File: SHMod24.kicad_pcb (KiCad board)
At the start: 2 copper layers, 49.5 x 49.5 mm, 34 parts, among them IC1 ArduinoProMini, J1 Conn_01x01, J2 Conn_01x01, J3 Conn_01x01, J4 Conn_01x01, Q1 FS8205A, U1 ESP-12, U2 NRF24L01, U3 AP2112K-3.3, U4 TP4056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

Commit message: NRF ESP Jumper
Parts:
- removed J2, J3, J4: Conn_01x01, Pin_Headers:Pin_Header_Straight_1x01_Pitch2.54mm
- added J5: 12V, Connectors_Terminal_Blocks:TerminalBlock_Pheonix_MKDS1.5-2pol, B.Cu at (55.5, 96.5)
- added JP3: Jumper_DeepSleep, LeoDJ-kicad:SOLDER-JUMPER_1-WAY, F.Cu at (95.8, 136.6)
- added JP4: ESP NRF, LeoDJ-kicad:SOLDER-JUMPER_2-WAY, F.Cu at (75.6, 80.8)
- added JP5: ESP NRF, LeoDJ-kicad:SOLDER-JUMPER_2-WAY, F.Cu at (75.6, 82.5)
- added JP6: ESP NRF, LeoDJ-kicad:SOLDER-JUMPER_2-WAY, F.Cu at (75.6, 79.0)
- added JP7: ESP NRF, LeoDJ-kicad:SOLDER-JUMPER_2-WAY, F.Cu at (75.6, 77.2)
- added JP8: ESP NRF, LeoDJ-kicad:SOLDER-JUMPER_2-WAY, F.Cu at (75.6, 75.4)
- added R11: 10k, Resistors_SMD:R_0805_HandSoldering, F.Cu at (107.7, 126.8)
- C1, C2, C3, C5, C6, C8, D1, JP1, L1, Q1, R10, R6, R7, R8, R9, U3, U4, U5, U6: moved to B.Cu
- J1: value Conn_01x01 -> Conn_02x06_Odd_Even; footprint Pin_Headers:Pin_Header_Straight_1x01_Pitch2.54mm -> Pin_Headers:Pin_Header_Straight_2x06_Pitch2.54mm_SMD
- moved J1 37.3 mm to (75.9, 105.7), turned to 90 degrees
- moved C7 34.3 mm to (59.2, 94.2), turned to 270 degrees
- moved C3 25.9 mm to (71.0, 106.8)
- moved C4 22.5 mm to (102.6, 126.8)
- moved R7 18.3 mm to (74.8, 109.9), turned to 180 degrees
- moved U5 18.3 mm to (74.8, 106.8), turned to 180 degrees
- moved C9 18.1 mm to (95.2, 129.6)
- moved Q1 17.8 mm to (75.1, 101.5), turned to 180 degrees
- moved R10 14.8 mm to (52.6, 106.5)
- moved R9 14.8 mm to (52.6, 103.3)
- moved C2 12.4 mm to (65.7, 97.5)
- moved C1 12.2 mm to (65.7, 91.2)
- moved R6 11.0 mm to (80.1, 96.4), turned to 270 degrees
- moved U4 10.7 mm to (75.1, 96.4), turned to 180 degrees
- moved JP1 10.5 mm to (69.3, 94.4), turned to 270 degrees
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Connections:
- net +VDC renamed P01
- net Net-(C6-Pad2) renamed /SW
- net Net-(R4-Pad2) renamed ADC
- U1 pad 10: Net-(U1-Pad10) -> GPIO15
- U1 pad 4: Net-(U1-Pad4) -> GPIO16
- U1 pad 5: Net-(U1-Pad5) -> GPIO14
- U1 pad 6: Net-(U1-Pad6) -> GPIO12
- U1 pad 7: Net-(U1-Pad7) -> GPIO13
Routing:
- net GPIO15: track 0.00 -> 32.4 mm, vias 0 -> 1
- net GPIO13: track 0.00 -> 12.2 mm, vias 0 -> 1
- net SCK: track 12.1 -> 23.0 mm
- net MISO: track 16.4 -> 27.0 mm, vias 0 -> 1
- net MOSI: track 20.4 -> 30.4 mm
- net GPIO14: track 0.00 -> 7.82 mm, vias 0 -> 1
- net GPIO16: track 0.00 -> 7.68 mm, vias 0 -> 1
- net GPIO12: track 0.00 -> 7.53 mm, vias 0 -> 1
- net Net-(Q1-Pad4): track 4.18 -> 9.99 mm
- net A0: track 20.6 -> 25.2 mm
- net /SW: track 13.6 -> 16.9 mm
- net SDA: track 39.4 -> 42.2 mm
- net +12V: track 13.4 -> 11.2 mm
- net SCL: track 36.3 -> 38.1 mm
- net TX: track 46.8 -> 47.8 mm
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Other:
- net class Power added: clearance 0.2, trace_width 0.4, via_dia 0.6, via_drill 0.4

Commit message: migrate to KiCad5 && further layouting
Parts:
- added ?: MountingHole_3.2mm_M3, Mounting_Holes:MountingHole_3.2mm_M3, F.Cu at (75.6, 65.4)
- added ?: MountingHole_3.2mm_M3, Mounting_Holes:MountingHole_3.2mm_M3, F.Cu at (54.0, 108.6)
- added ?: MountingHole_3.2mm_M3, Mounting_Holes:MountingHole_3.2mm_M3, F.Cu at (97.2, 108.6)
- added C10: 10µF, Capacitor_SMD:C_0805_2012Metric, F.Cu at (86.4, 84.1)
- added D2: LED, LED_SMD:LED_0805_2012Metric, B.Cu at (69.4, 101.6)
- added J2: Conn_01x01, Connector_Wire:SolderWirePad_1x01_Drill0.8mm, F.Cu at (52.8, 103.9)
- added J3: Conn_01x01, Connector_Wire:SolderWirePad_1x01_Drill0.8mm, F.Cu at (52.8, 100.8)
- added R12: 10k, Resistor_SMD:R_0805_2012Metric, F.Cu at (57.8, 117.8)
- added R13: 10k, Resistor_SMD:R_0805_2012Metric, F.Cu at (61.6, 117.8)
- added R14: 1k, Resistor_SMD:R_0805_2012Metric, B.Cu at (72.8, 101.6)
- added U7: NRF24L01, mysensors_radios:NRF24L01-SMD, F.Cu at (90.8, 63.9)
- C1, C2, C3: footprint Capacitors_SMD:C_0805_HandSoldering -> Capacitor_SMD:C_0805_2012Metric
- C4: footprint Capacitors_SMD:C_0805_HandSoldering -> Capacitor_SMD:C_0805_2012Metric; moved to B.Cu
- C5, C6: footprint Capacitors_SMD:C_0805 -> Capacitor_SMD:C_0805_2012Metric
- C7, C8: footprint Capacitors_SMD:C_1210 -> Capacitor_SMD:C_1210_3225Metric
- C9: footprint Capacitors_SMD:CP_Elec_6.3x5.8 -> Capacitor_SMD:CP_Elec_6.3x5.8
- D1: footprint Diodes_SMD:D_SMA -> Diode_SMD:D_SMA
- J1: footprint Pin_Headers:Pin_Header_Straight_2x06_Pitch2.54mm_SMD -> Connector_PinHeader_2.54mm:PinHeader_2x06_P2.54mm_Vertical_SMD
- J5: footprint Connectors_Terminal_Blocks:TerminalBlock_Pheonix_MKDS1.5-2pol -> TerminalBlock_Phoenix:TerminalBlock_Phoenix_MKDS-1,5-2_1x02_P5.00mm_Horizontal
- JP1: footprint jumper:SOLDER-JUMPER_2-WAY -> LeoDJ-kicad:SOLDER-JUMPER_2-WAY
- L1: footprint LeoDJ:L_0630 -> LeoDJ-kicad:L_0630
- Q1: footprint Housings_SSOP:TSSOP-8_4.4x3mm_Pitch0.65mm -> Package_SO:TSSOP-8_4.4x3mm_P0.65mm
- R1, R11, R2, R3, R4, R5, R6, R7, R8: footprint Resistors_SMD:R_0805_HandSoldering -> Resistor_SMD:R_0805_2012Metric
- R10, R9: footprint Resistors_SMD:R_0805 -> Resistor_SMD:R_0805_2012Metric
- U3: footprint TO_SOT_Packages_SMD:SOT-23-5 -> Package_TO_SOT_SMD:SOT-23-5
- U4: footprint Housings_SOIC:SOIC-8_3.9x4.9mm_Pitch1.27mm -> Package_SO:SOIC-8_3.9x4.9mm_P1.27mm
- U5, U6: footprint TO_SOT_Packages_SMD:SOT-23-6_Handsoldering -> Package_TO_SOT_SMD:SOT-23-6_Handsoldering
- moved JP3 66.3 mm to (72.1, 74.7), turned to 270 degrees
- moved R11 61.5 mm to (61.3, 86.4), turned to 180 degrees
- moved C9 46.4 mm to (65.8, 93.7), turned to 90 degrees
- moved C4 40.8 mm to (65.9, 109.1), turned to 270 degrees
- moved R10 27.0 mm to (76.1, 93.2), turned to 90 degrees
- moved C6 24.8 mm to (72.7, 90.5), turned to 180 degrees
- moved R9 24.5 mm to (76.1, 96.5), turned to 90 degrees
- moved U6 21.0 mm to (72.7, 93.3), turned to 180 degrees
- moved D1 19.3 mm to (67.2, 90.5), turned to 180 degrees
- moved C8 17.7 mm to (72.7, 96.7), turned to 0 degrees
- moved C2 16.3 mm to (81.0, 102.9), turned to 270 degrees
- moved C1 15.4 mm to (75.7, 102.9), turned to 270 degrees
- moved U3 15.3 mm to (78.4, 102.9), turned to 90 degrees
- moved R8 13.0 mm to (65.9, 105.5)
- moved Q1 13.0 mm to (62.1, 102.0)
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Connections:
- net +12V renamed VCC
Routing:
- net +BATT: track 0.00 -> 47.8 mm
- net N24_CS: track 13.8 -> 38.8 mm, vias 2 -> 3
- net N24_CE: track 14.4 -> 37.9 mm, vias 1 -> 2
- net VCC: track 11.2 -> 31.1 mm
- net MOSI: track 30.4 -> 39.4 mm
- net SCK: track 23.0 -> 31.5 mm
- net MISO: track 27.0 -> 35.5 mm
- net +5V: track 32.9 -> 39.8 mm, vias 0 -> 1
- net Net-(D2-Pad1): track 0.00 -> 5.94 mm
- net GPIO16: track 7.68 -> 12.9 mm, vias 1 -> 2
- net Net-(JP3-Pad1): track 0.00 -> 4.19 mm, vias 0 -> 1
- net -BATT: track 16.6 -> 19.8 mm
- net GPIO15: track 32.4 -> 35.6 mm
- net A0: track 25.2 -> 28.1 mm
- net GND: track 64.4 -> 62.1 mm, vias 1 -> 5
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- added copper zone on F.Cu, net GND

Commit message: more layouting
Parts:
- removed ? (x3): MountingHole_3.2mm_M3, Mounting_Holes:MountingHole_3.2mm_M3
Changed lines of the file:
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@@
     (tracks 431)
     (zones 0)
-    (modules 50)
+    (modules 47)
     (nets 74)
   )
@@
     )
   )
-  (module Mounting_Holes:MountingHole_3.2mm_M3 (layer F.Cu)
-    (at 75.565 65.405)
-    (descr "Mounting Hole 3.2mm, no annular, M3")
-    (tags "mounting hole 3.2mm no annular m3")
-    (attr virtual)
-    (fp_text reference "" (at 0 -4.2) (layer F.SilkS)
-      (effects (font (size 1 1) (thickness 0.15)))
-    )
-    (fp_text value MountingHole_3.2mm_M3 (at 0 4.2) (layer F.Fab)
-      (effects (font (size 1 1) (thickness 0.15)))
-    )
-    (fp_text user %R (at 0.3 0) (layer F.Fab)
-      (effects (font (size 1 1) (thickness 0.15)))
-    )
-    (fp_circle (center 0 0) (end 3.2 0) (layer Cmts.User) (width 0.15))
-    (fp_circle (center 0 0) (end 3.45 0) (layer F.CrtYd) (width 0.05))
-    (pad 1 np_thru_hole circle (at 0 0) (size 3.2 3.2) (drill 3.2) (layers *.Cu *.Mask))
-  )
-  (module Mounting_Holes:MountingHole_3.2mm_M3 (layer F.Cu)
-    (at 53.975 108.585)
-    (descr "Mounting Hole 3.2mm, no annular, M3")
-    (tags "mounting hole 3.2mm no annular m3")
-    (attr virtual)
-    (fp_text reference "" (at 0 -4.2) (layer F.SilkS)
-      (effects (font (size 1 1) (thickness 0.15)))
-    )
-    (fp_text value MountingHole_3.2mm_M3 (at 0 4.2) (layer F.Fab)
-      (effects (font (size 1 1) (thickness 0.15)))
-    )
-    (fp_text user %R (at 0.3 0) (layer F.Fab)
-      (effects (font (size 1 1) (thickness 0.15)))
-    )
-    (fp_circle (center 0 0) (end 3.2 0) (layer Cmts.User) (width 0.15))
-    (fp_circle (center 0 0) (end 3.45 0) (layer F.CrtYd) (width 0.05))
-    (pad 1 np_thru_hole circle (at 0 0) (size 3.2 3.2) (drill 3.2) (layers *.Cu *.Mask))
-  )
   (module mysensors_arduino:pro_mini (layer B.Cu)
     (at 90.805 80.01 270)
@@
     (pad 2 smd rect (at 0 0) (size 1 1) (layers F.Cu F.Paste F.Mask)
       (net 51 GPIO15))
-  )
-  (module Mounting_Holes:MountingHole_3.2mm_M3 (layer F.Cu)
-    (at 97.155 108.585)
-    (descr "Mounting Hole 3.2mm, no annular, M3")
-    (tags "mounting hole 3.2mm no annular m3")
-    (attr virtual)
-    (fp_text reference "" (at 0 -4.2) (layer F.SilkS)
-      (effects (font (size 1 1) (thickness 0.15)))
-    )
-    (fp_text value MountingHole_3.2mm_M3 (at 0 4.2) (layer F.Fab)
-      (effects (font (size 1 1) (thickness 0.15)))
-    )
-    (fp_text user %R (at 0.3 0) (layer F.Fab)
-      (effects (font (size 1 1) (thickness 0.15)))
-    )
-    (fp_circle (center 0 0) (end 3.2 0) (layer Cmts.User) (width 0.15))
-    (fp_circle (center 0 0) (end 3.45 0) (layer F.CrtYd) (width 0.05))
-    (pad 1 np_thru_hole circle (at 0 0) (size 3.2 3.2) (drill 3.2) (layers *.Cu *.Mask))
   )
   (module Capacitor_SMD:C_0805_2012Metric (layer B.Cu)
@@
   (segment (start 74.0575 91.7105) (end 74.0575 92.3315) (width 0.25) (layer B.Cu) (net 48))
   (segment (start 73.7075 91.3605) (end 74.0575 91.7105) (width 0.25) (layer B.Cu) (net 48))
-  (segment (start 71.3575 93.2815) (end 71.3575 94.2315) (width 0.4) (layer B.Cu) (net 71))
-  (segment (start 59.262 91.52) (end 55.499 91.52) (width 0.4) (layer B.Cu) (net 71))
-  (segment (start 60.706 92.964) (end 59.262 91.52) (width 0.4) (layer B.Cu) (net 71))
-  (segment (start 71.3575 93.2815) (end 66.6115 93.2815) (width 0.4) (layer B.Cu) (net 71))
-  (segment (start 64.77 95.123) (end 64.77 97.79) (width 0.4) (layer B.Cu) (net 71))
-  (segment (start 66.6115 93.2815) (end 64.77 95.123) (width 0.4) (layer B.Cu) (net 71))
-  (segment (start 64.77 97.79) (end 64.008 98.552) (width 0.4) (layer B.Cu) (net 71))
-  (segment (start 64.008 98.552) (end 61.468 98.552) (width 0.4) (layer B.Cu) (net 71))
-  (segment (start 60.706 97.79) (end 60.706 92.964) (width 0.4) (layer B.Cu) (net 71))
-  (segment (start 61.468 98.552) (end 60.706 97.79) (width 0.4) (layer B.Cu) (net 71))
-  (segment (start 57.337477 91.52) (end 55.499 91.52) (width 0.4) (layer F.Cu) (net 71))
-  (segment (start 58.908 91.52) (end 57.337477 91.52) (width 0.4) (layer F.Cu) (net 71))
-  (segment (start 59.182 91.794) (end 58.908 91.52) (width 0.4) (layer F.Cu) (net 71))
-  (segment (start 59.182 92.804) (end 59.182 91.794) (width 0.4) (layer F.Cu) (net 71))
   (segment (start 76.1365 93.8505) (end 76.1365 95.1255) (width 0.25) (layer B.Cu) (net 49))
   (segment (start 74.191 94.098) (end 74.0575 94.2315) (width 0.25) (layer B.Cu) (net 49))
@@
   (segment (start 68.8975 74.6125) (end 68.8975 74.7075) (width 0.25) (layer B.Cu) (net 69) (status 30))
   (segment (start 60.0875 74.6125) (end 63.7375 74.6125) (width 0.25) (layer F.Cu) (net 69))
+  (segment (start 71.3575 93.2815) (end 71.3575 94.2315) (width 0.4) (layer B.Cu) (net 71))
+  (segment (start 59.262 91.52) (end 55.499 91.52) (width 0.4) (layer B.Cu) (net 71))
+  (segment (start 60.706 92.964) (end 59.262 91.52) (width 0.4) (layer B.Cu) (net 71))
+  (segment (start 71.3575 93.2815) (end 66.6115 93.2815) (width 0.4) (layer B.Cu) (net 71))
+  (segment (start 64.77 95.123) (end 64.77 97.79) (width 0.4) (layer B.Cu) (net 71))
+  (segment (start 66.6115 93.2815) (end 64.77 95.123) (width 0.4) (layer B.Cu) (net 71))
+  (segment (start 64.77 97.79) (end 64.008 98.552) (width 0.4) (layer B.Cu) (net 71))
+  (segment (start 64.008 98.552) (end 61.468 98.552) (width 0.4) (layer B.Cu) (net 71))
+  (segment (start 60.706 97.79) (end 60.706 92.964) (width 0.4) (layer B.Cu) (net 71))
+  (segment (start 61.468 98.552) (end 60.706 97.79) (width 0.4) (layer B.Cu) (net 71))
+  (segment (start 57.337477 91.52) (end 55.499 91.52) (width 0.4) (layer F.Cu) (net 71))
+  (segment (start 58.908 91.52) (end 57.337477 91.52) (width 0.4) (layer F.Cu) (net 71))
+  (segment (start 59.182 91.794) (end 58.908 91.52) (width 0.4) (layer F.Cu) (net 71))
+  (segment (start 59.182 92.804) (end 59.182 91.794) (width 0.4) (layer F.Cu) (net 71))
   (segment (start 68.5165 106.807) (end 67.7545 106.045) (width 0.25) (layer B.Cu) (net 72))
   (segment (start 68.9915 106.807) (end 68.5165 106.807) (width 0.25) (layer B.Cu) (net 72))

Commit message: even more layouting
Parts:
- J1: value Conn_02x06_Odd_Even -> Conn_02x14_Odd_Even; footprint Connector_PinHeader_2.54mm:PinHeader_2x06_P2.54mm_Vertical_SMD -> Connector_PinHeader_2.54mm:PinHeader_2x14_P2.54mm_Vertical_SMD
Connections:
- IC1 pad 12: Net-(IC1-Pad12) -> P09
- IC1 pad 13: Net-(IC1-Pad13) -> P10
- IC1 pad 18: Net-(IC1-Pad18) -> A1
- IC1 pad 19: Net-(IC1-Pad19) -> A2
- IC1 pad 20: Net-(IC1-Pad20) -> A3
- IC1 pad 5: Net-(IC1-Pad5) -> P02
- IC1 pad 6: Net-(IC1-Pad6) -> P03
- IC1 pad 7: Net-(IC1-Pad7) -> P04
- IC1 pad 8: Net-(IC1-Pad8) -> P05
- IC1 pad 9: Net-(IC1-Pad9) -> P06
- J1 pad 1: P01 -> GND
- J1 pad 10: P08 -> SCL
- J1 pad 11: P06 -> MISO
- J1 pad 12: P07 -> MOSI
- J1 pad 2: Net-(J1-Pad2) -> GND
- J1 pad 3: P02 -> +5V
- J1 pad 4: P11 -> VCC
- J1 pad 5: P03 -> +3V3
- J1 pad 6: P10 -> +3V3
- J1 pad 7: P04 -> RX
- J1 pad 8: P09 -> TX
- J1 pad 9: P05 -> SDA
- JP4 pad 1: GPIO13 -> Net-(JP4-Pad1)
- JP4 pad 2: GPIO13 -> Net-(JP4-Pad1)
- JP4 pad 3: MOSI -> Net-(JP4-Pad3)
- JP5 pad 1: GPIO12 -> Net-(JP5-Pad1)
- JP5 pad 2: GPIO12 -> Net-(JP5-Pad1)
- JP5 pad 3: MISO -> Net-(JP5-Pad3)
- JP6 pad 1: GPIO14 -> Net-(JP6-Pad1)
- JP6 pad 2: GPIO14 -> Net-(JP6-Pad1)
- JP6 pad 3: SCK -> Net-(JP6-Pad3)
- JP7 pad 1: GPIO16 -> Net-(JP7-Pad1)
- JP7 pad 2: GPIO16 -> Net-(JP7-Pad1)
- JP7 pad 3: N24_CE -> Net-(JP7-Pad3)
- JP8 pad 1: GPIO15 -> Net-(JP8-Pad1)
- JP8 pad 2: GPIO15 -> Net-(JP8-Pad1)
- JP8 pad 3: N24_CS -> Net-(JP8-Pad3)

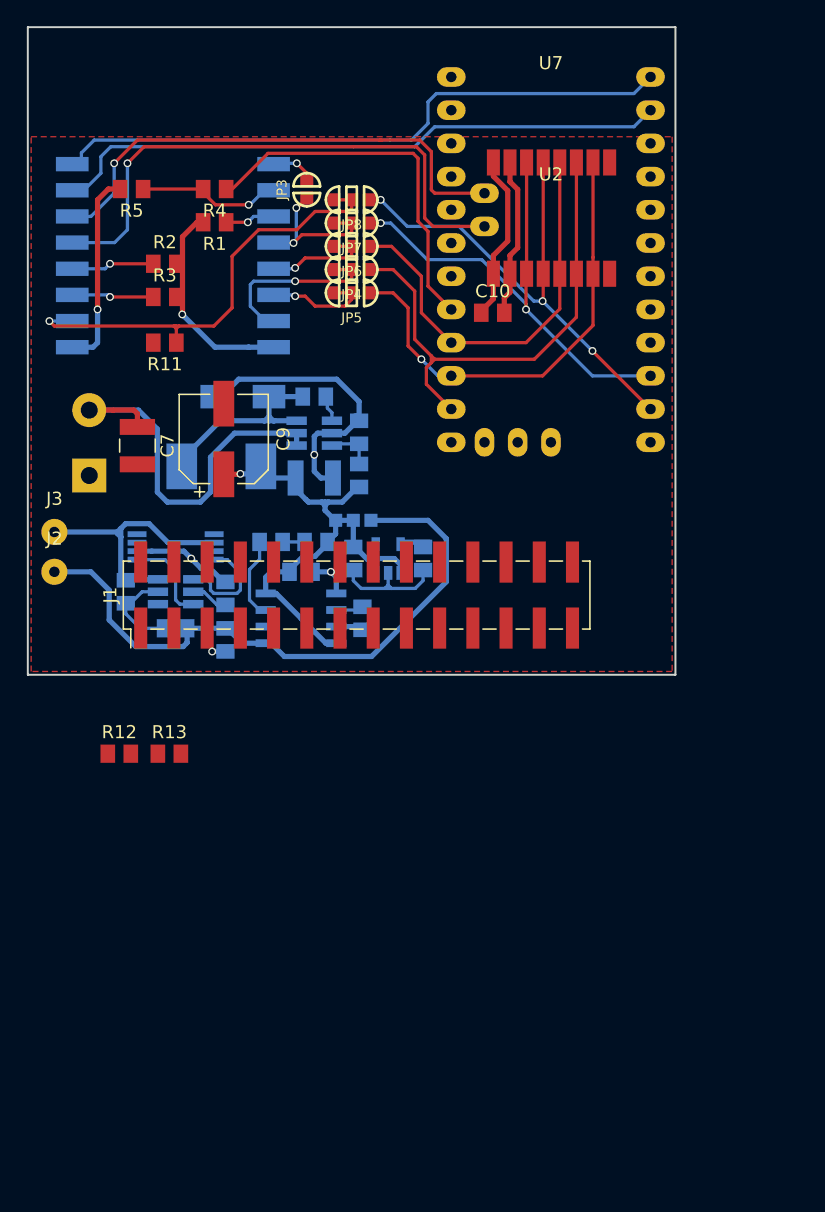
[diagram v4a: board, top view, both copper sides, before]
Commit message: layouting of the current schematic complete
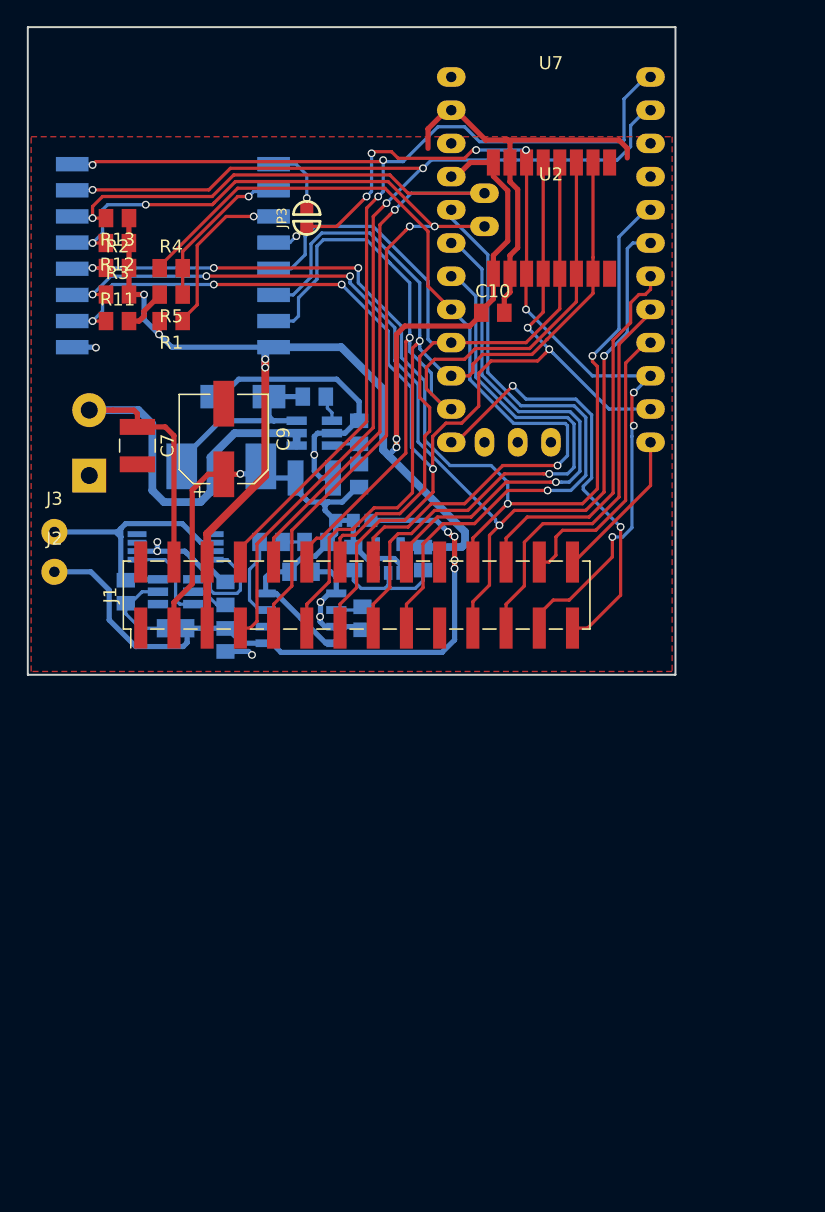
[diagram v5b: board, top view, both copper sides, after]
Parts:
- removed JP4, JP5, JP6, JP7, JP8: ESP NRF, LeoDJ-kicad:SOLDER-JUMPER_2-WAY
- moved R13 41.2 mm to (57.7, 76.8), turned to 180 degrees
- moved R12 39.1 mm to (57.6, 78.7), turned to 180 degrees
- moved R5 8.63 mm to (61.8, 82.7)
- moved R1 8.26 mm to (61.8, 84.7)
- moved R4 6.90 mm to (61.8, 80.7), turned to 0 degrees
- moved R11 3.98 mm to (57.7, 84.7), turned to 0 degrees
- moved R2 3.63 mm to (57.7, 80.6)
- moved R3 3.62 mm to (57.7, 82.7)
- moved JP3 2.16 mm to (72.1, 76.8)
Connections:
- IC1 pad 10: N24_CE -> GPIO16
- IC1 pad 11: N24_CS -> CS
- IC1 pad 14: MOSI -> GPIO13
- IC1 pad 15: MISO -> GPIO12
- IC1 pad 16: SCK -> GPIO14
- IC1 pad 5: P02 -> GPIO0
- IC1 pad 6: P03 -> GPIO2
- J1 pad 11: MISO -> GPIO12
- J1 pad 12: MOSI -> GPIO13
- J1 pad 14: SCK -> GPIO14
- J1 pad 21: P03 -> GPIO2
- J1 pad 22: P02 -> GPIO0
- J1 pad 25: P07 -> GPIO16
- R11 pad 1: GPIO15 -> CS
- U1 pad 10: GPIO15 -> CS
- U2 pad 3: N24_CE -> GPIO16
- U2 pad 4: N24_CS -> CS
- U2 pad 5: SCK -> GPIO14
- U2 pad 6: MOSI -> GPIO13
- U2 pad 7: MISO -> GPIO12
- U7 pad 3: N24_CE -> GPIO16
- U7 pad 4: N24_CS -> CS
- U7 pad 5: SCK -> GPIO14
- U7 pad 6: MOSI -> GPIO13
- U7 pad 7: MISO -> GPIO12
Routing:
- net CS: track 0.00 -> 96.9 mm, vias 0 -> 6
- net GPIO2: track 5.10 -> 85.0 mm, vias 1 -> 5
- net GPIO0: track 5.19 -> 83.3 mm, vias 1 -> 5
- net +3V3: track 30.7 -> 108.1 mm, vias 1 -> 6
- net GPIO12: track 9.09 -> 76.3 mm
- net GPIO13: track 13.6 -> 77.9 mm
- net GPIO16: track 12.9 -> 73.1 mm, vias 2 -> 9
- net GPIO14: track 9.10 -> 67.7 mm, vias 1 -> 0
- net A3: track 0.00 -> 48.5 mm, vias 0 -> 1
- net A1: track 0.00 -> 44.6 mm, vias 0 -> 1
- net RX: track 46.8 -> 89.2 mm, vias 0 -> 3
- net A2: track 0.00 -> 40.8 mm, vias 0 -> 1
- net A0: track 28.1 -> 68.8 mm, vias 0 -> 1
- net MOSI: track 39.4 -> 0.00 mm
- net N24_CS: track 38.8 -> 0.00 mm, vias 3 -> 0
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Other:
- net class Power+ added: clearance 0.2, trace_width 0.6, via_dia 0.6, via_drill 0.4

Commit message: move component references
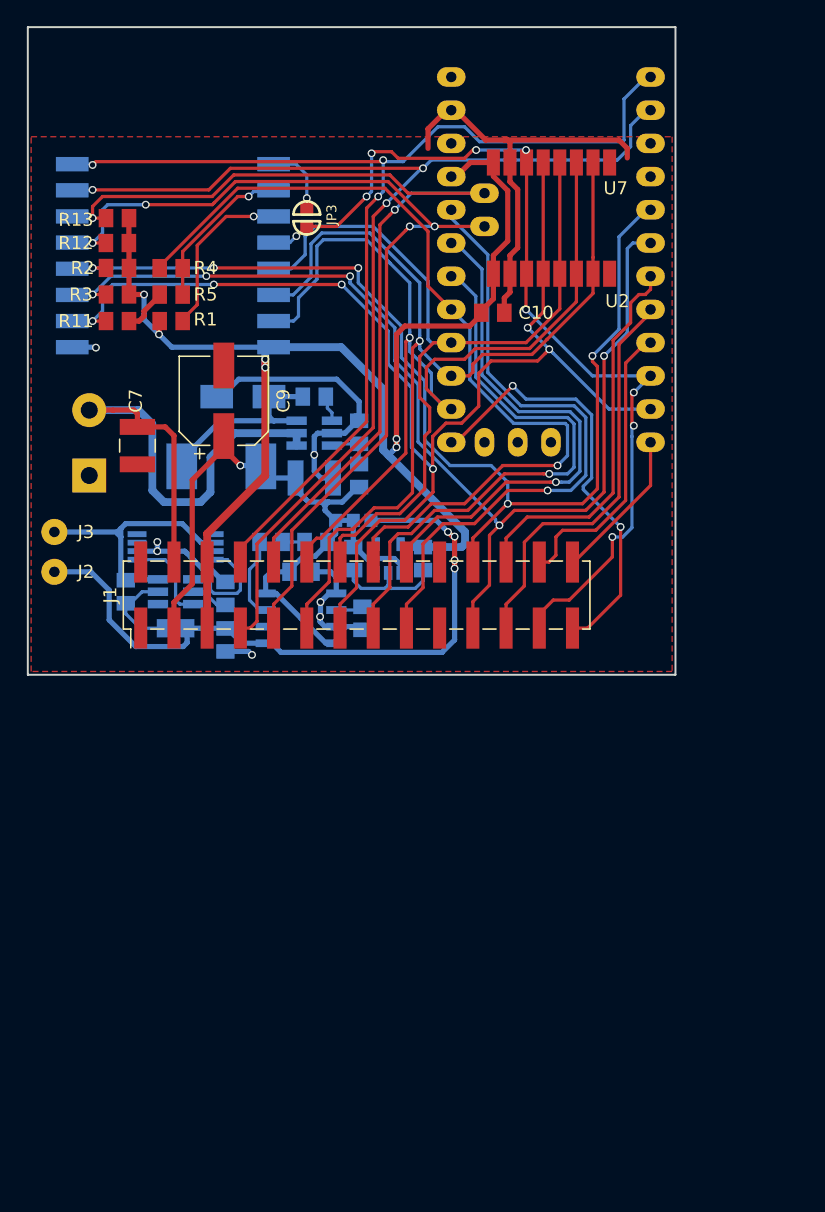
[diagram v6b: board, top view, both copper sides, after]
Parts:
- moved C9 2.92 mm to (65.8, 90.8)
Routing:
- net +5V: track 53.8 -> 57.3 mm
